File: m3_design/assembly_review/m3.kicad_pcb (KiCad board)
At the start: 4 copper layers, 46 x 90 mm, 245 parts, among them J1 DB125-3.5-2P-GN-S, J121 DB125-3.5-2P-BK-S, J122 SERVO 3x4, J123 BM02B-GHS-TBT(LF)(SN), J124 DB125-3.5-2P-BK-S, J2 TC2030-IDC-NL SWD, J3 USB-C 2.0, J400 BM02B-GHS-TBT(LF)(SN), J410 GPS 4V8/GND/TX/RX, J420 RADIO 4V8/GND/TX/RX, J9 CAMERA 5V/GND/RX/TX, Q120 AON6403, Q121 AON6403, Q122 AO3400A, Q123 AO3400A, Q124 AON7524, U1 STM32H743VIT6, U10 TPS2553DBVR, U11 TPS2121RUXR, U12 TXU0202DCUR, U13 TPS70933DBVR, U2 AP63203WU-7, U3 W25Q128JVSIQ, U4 LSM6DSV320X, U400 AP63201WU-7, U401 TPS7A9101DSKR, U402 TPS2553DBVR, U410 TPS2553DBVR, U411 TXU0202DCUR, U412 TPS70933DBVR, U420 TPS2553DBVR, U421 TXU0202DCUR, U422 TPS70933DBVR, U5 MS561101BA03, U9 TPS259470LRPWR, Y1 25MHz CL8pF

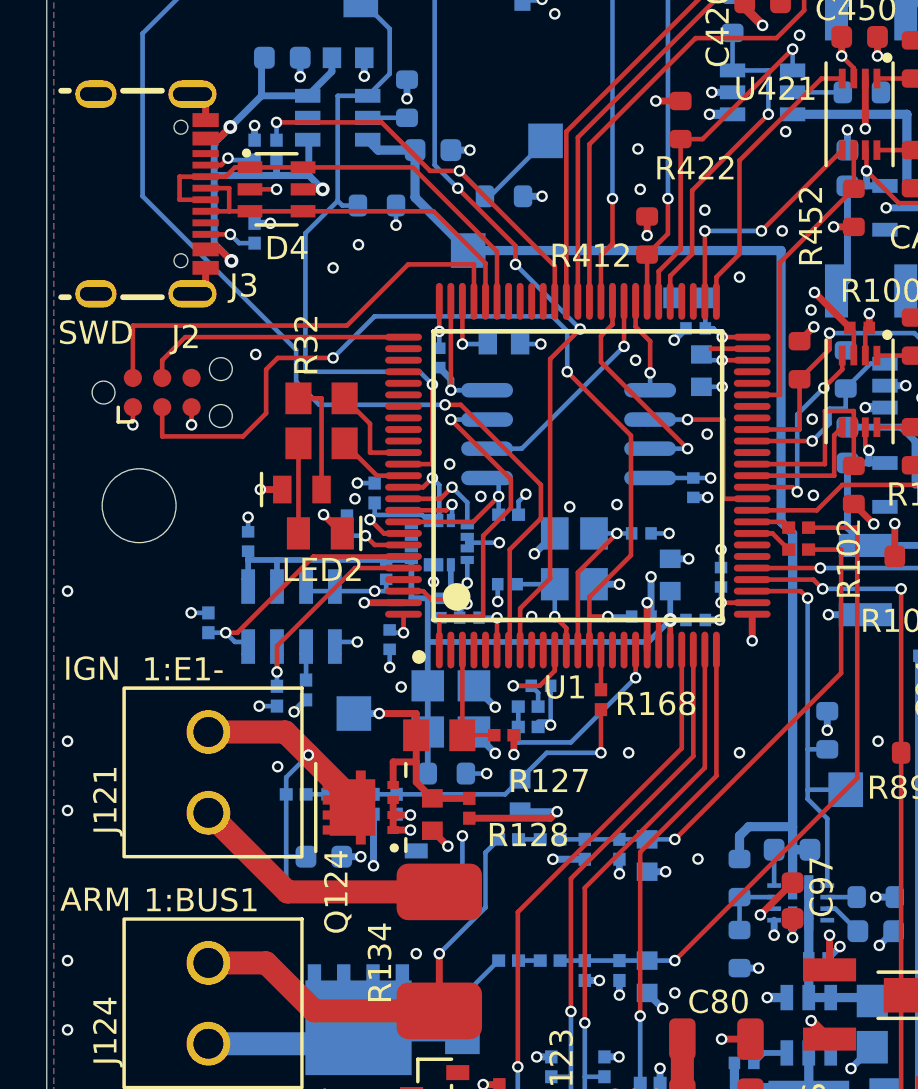
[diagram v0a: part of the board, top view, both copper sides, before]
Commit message: R10 review round 8 and fix pass: ten-lens review of b242ab8e (0 Critical, 3 Major, 22 Minor); check.sh fail-closed test repaired and run; ORDERING 8 U5 coat exclusion and complete R10 order remarks; gates: legend text, hidden safety designators, K-width, fab manifest binding in check.sh; copper clean-ups (VBUS_SENSE jog, In2 3V3 neck / tooth, I2C stitch via); board 407d1d84..., check.sh 0
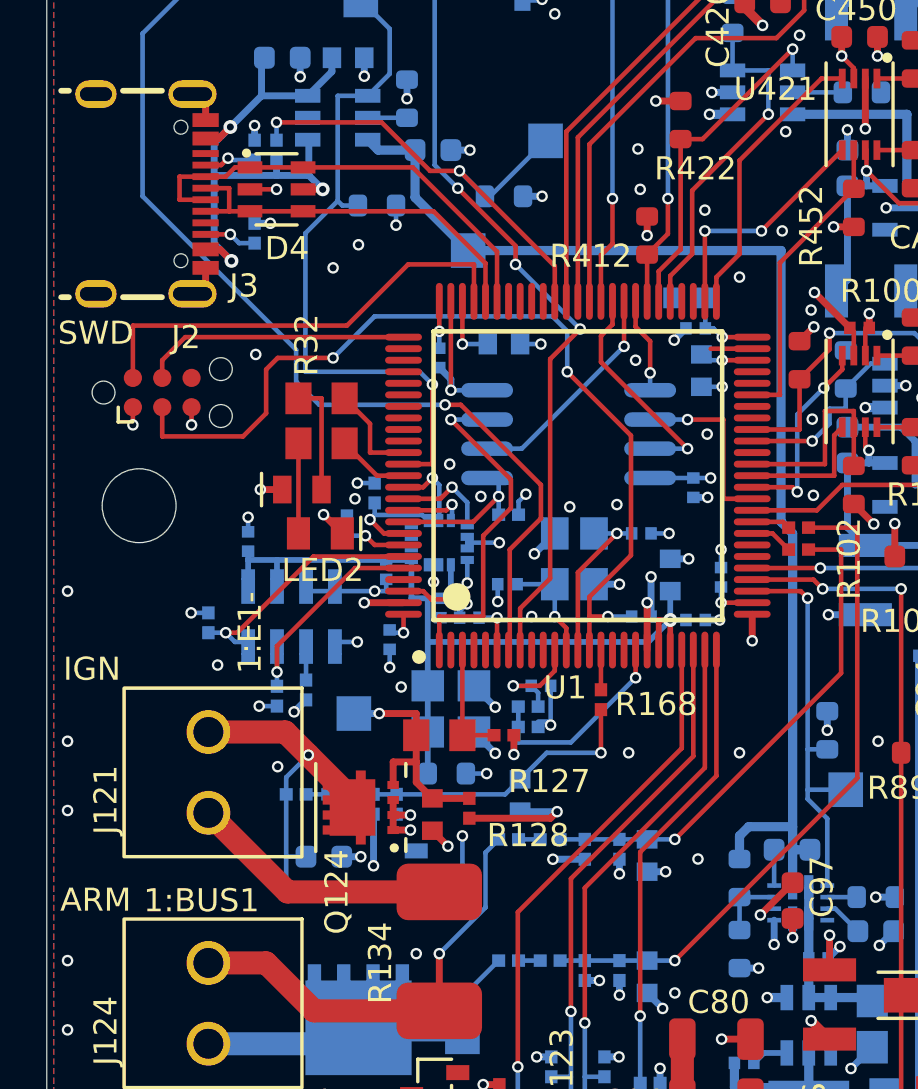
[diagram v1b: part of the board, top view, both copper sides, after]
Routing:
- net GND: track 186.4 -> 186.8 mm, vias 210 -> 211
